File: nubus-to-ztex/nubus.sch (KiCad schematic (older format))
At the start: 46 parts, among them J4 C96ABC, U1 74LVT125, U12 74CB3T1G125DBVR, U13 SN74CB3T3125PWR, U14 SN74CB3T3245PWR, U2 74LVT125, U3 74LVT125, U4 SN74CB3T3125PWR, U5 74LVT245BPW,118, U6 74LVT245BPW,118, U7 74LVT245BPW,118, U8 74LVT245BPW,118

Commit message: cleanups, alternative MPN for 2x32 headers (TBC)
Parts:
- J4: MPN 85003-0567 -> 0850030567; MPN alias (none) -> 85003-0567
- U12: value 74CB3T1G125DBVR -> SN74CB3T1G125DBVR; MPN 74CB3T1G125DBVR -> SN74CB3T1G125DBVR
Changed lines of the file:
@@
 F 2 "For_SeeedStudio:DIN41612_C_3x32_Male_Horizontal_THT" H 22250 5800 50  0001 C CNN
 F 3 " ~" H 22250 5800 50  0001 C CNN
-F 4 "85003-0567" H 22250 5750 50  0001 C CNN "MPN"
+F 4 "85003-0567" H 22250 5750 50  0001 C CNN "MPN alias"
 F 5 "https://www.mouser.fr/ProductDetail/Molex/85003-0567?qs=U4pz39agNJB6P1oBpJ4bJA%3D%3D" H 22250 5750 50  0001 C CNN "URL"
 F 6 "DIN-096CPC-RR1-HM" H 22250 5750 50  0001 C CNN "MPN (3M)"
@@
 F 8 "09033967921" H 22250 5750 50  0001 C CNN "MPN (Harting)"
 F 9 "09033966921" H 22250 5750 50  0001 C CNN "MPN (Harting 2)"
+F 10 "0850030567" H 22250 5750 50  0001 C CNN "MPN"
 	1    22250 5750
 	1    0    0    -1
@@
 P 7450 13450
 F 0 "U12" H 7450 13767 50  0000 C CNN
-F 1 "74CB3T1G125DBVR" H 7450 13676 50  0000 C CNN
+F 1 "SN74CB3T1G125DBVR" H 7450 13676 50  0000 C CNN
 F 2 "Package_TO_SOT_SMD:SOT-23-5" H 7450 13450 50  0001 C CNN
 F 3 "http://www.ti.com/lit/sg/scyt129e/scyt129e.pdf" H 7450 13450 50  0001 C CNN
-F 4 "74CB3T1G125DBVR" H 7450 13450 50  0001 C CNN "MPN"
+F 4 "SN74CB3T1G125DBVR" H 7450 13450 50  0001 C CNN "MPN"
 F 5 "https://www.lcsc.com/product-detail/Analog-Switches-Multiplexers_Texas-Instruments-SN74CB3T1G125DBVR_C134001.html" H 7450 13450 50  0001 C CNN "URL"
 	1    7450 13450

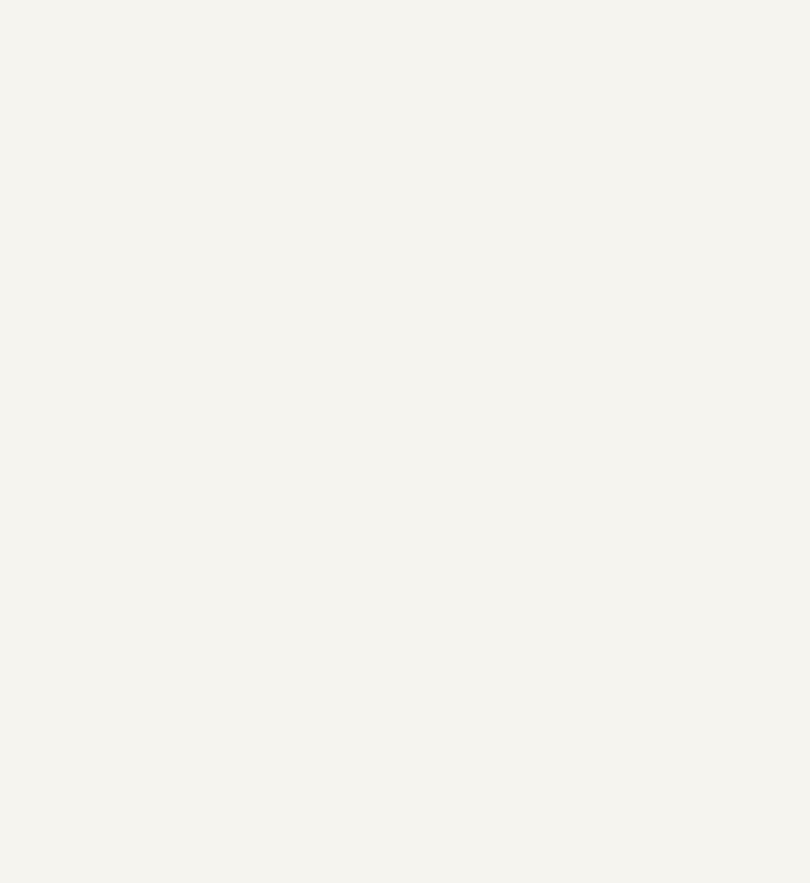
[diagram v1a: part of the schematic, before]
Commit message: reinstate some useful debug LEDs
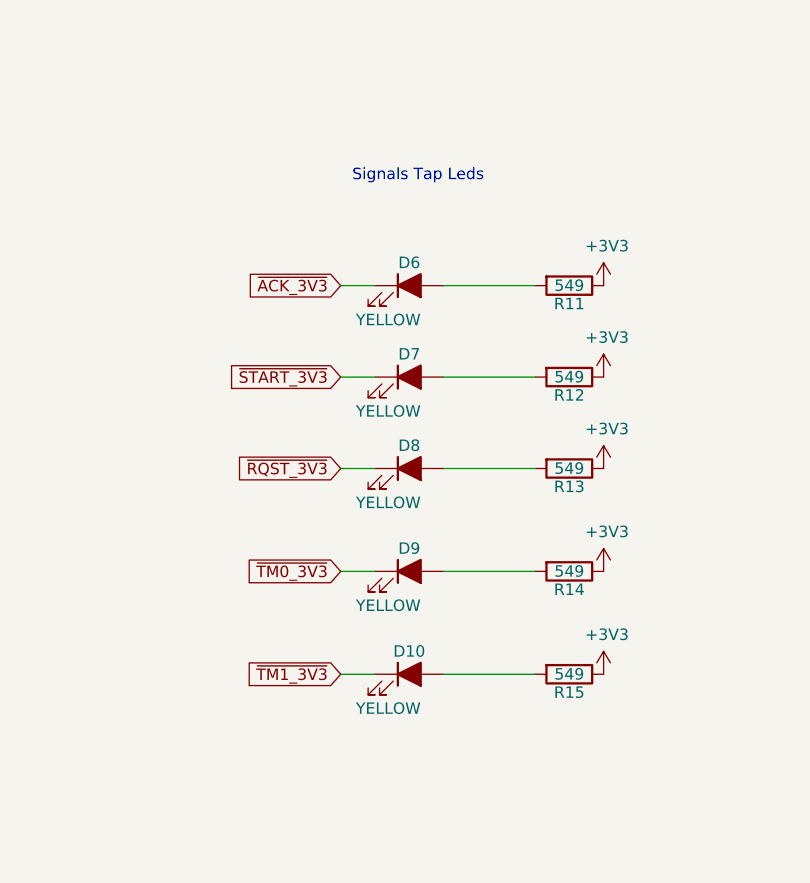
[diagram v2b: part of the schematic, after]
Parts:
- added D10, D6, D7, D8, D9: YELLOW, LED_SMD:LED_0805_2012Metric, symbol Device:LED_ALT
- added R11, R12, R13, R14, R15: 549, Resistor_SMD:R_0603_1608Metric, symbol Device:R
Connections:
- wire segments 54 -> 64
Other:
- note added: "Signals Tap Leds"

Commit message: cut down brightness of LEDs, more 2x32 pin headers reference
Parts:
- R11, R12, R13, R14, R15, R16, R17, R18, R19: value 549 -> 590; MPN 0603WAF5490T5E -> 0603WAF5900T5E; URL https://lcsc.com/product-detail/Chip-Resistor-Surface-Mount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 -> https://www.lcsc.com/product-detail/Chip-Resistor-Surface-M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
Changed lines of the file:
@@
 $Descr A2 23386 16535
 encoding utf-8
-Sheet 3 9
+Sheet 3 10
 Title "nubus-to-ztex NuBus connection & level shifting"
 Date ""
@@
 AR Path="/618F532C/61D85DF0" Ref="R16"  Part="1"
 F 0 "R16" V 16830 7850 50  0000 C CNN
-F 1 "549" V 16750 7850 50  0000 C CNN
+F 1 "590" V 16750 7850 50  0000 C CNN
 F 2 "Resistor_SMD:R_0603_1608Metric" V 16680 7850 50  0001 C CNN
 F 3 "" H 16750 7850 50  0000 C CNN
-F 4 "0603WAF5490T5E" V 16750 7850 50  0001 C CNN "MPN"
-F 5 "https://lcsc.com/product-detail/Chip-Resistor-Surface-Mount_UNI-ROYAL-Uniroyal-Elec-0603WAF5490T5E_C23079.html" V 16750 7850 50  0001 C CNN "URL"
+F 4 "0603WAF5900T5E" V 16750 7850 50  0001 C CNN "MPN"
+F 5 "https://www.lcsc.com/product-detail/Chip-Resistor-Surface-Mount_UNI-ROYAL-Uniroyal-Elec-0603WAF5900T5E_C23084.html" V 16750 7850 50  0001 C CNN "URL"
 	1    16750 7850
 	0    1    1    0
@@
 AR Path="/618F532C/61D85E0D" Ref="R17"  Part="1"
 F 0 "R17" V 16830 8350 50  0000 C CNN
-F 1 "549" V 16750 8350 50  0000 C CNN
+F 1 "590" V 16750 8350 50  0000 C CNN
 F 2 "Resistor_SMD:R_0603_1608Metric" V 16680 8350 50  0001 C CNN
 F 3 "" H 16750 8350 50  0000 C CNN
-F 4 "0603WAF5490T5E" V 16750 8350 50  0001 C CNN "MPN"
-F 5 "https://lcsc.com/product-detail/Chip-Resistor-Surface-Mount_UNI-ROYAL-Uniroyal-Elec-0603WAF5490T5E_C23079.html" V 16750 8350 50  0001 C CNN "URL"
+F 4 "0603WAF5900T5E" V 16750 8350 50  0001 C CNN "MPN"
+F 5 "https://www.lcsc.com/product-detail/Chip-Resistor-Surface-Mount_UNI-ROYAL-Uniroyal-Elec-0603WAF5900T5E_C23084.html" V 16750 8350 50  0001 C CNN "URL"
 	1    16750 8350
 	0    1    1    0
@@
 AR Path="/618F532C/61D85E2A" Ref="R18"  Part="1"
 F 0 "R18" V 16830 8850 50  0000 C CNN
-F 1 "549" V 16750 8850 50  0000 C CNN
+F 1 "590" V 16750 8850 50  0000 C CNN
 F 2 "Resistor_SMD:R_0603_1608Metric" V 16680 8850 50  0001 C CNN
 F 3 "" H 16750 8850 50  0000 C CNN
-F 4 "0603WAF5490T5E" V 16750 8850 50  0001 C CNN "MPN"
-F 5 "https://lcsc.com/product-detail/Chip-Resistor-Surface-Mount_UNI-ROYAL-Uniroyal-Elec-0603WAF5490T5E_C23079.html" V 16750 8850 50  0001 C CNN "URL"
+F 4 "0603WAF5900T5E" V 16750 8850 50  0001 C CNN "MPN"
+F 5 "https://www.lcsc.com/product-detail/Chip-Resistor-Surface-Mount_UNI-ROYAL-Uniroyal-Elec-0603WAF5900T5E_C23084.html" V 16750 8850 50  0001 C CNN "URL"
 	1    16750 8850
 	0    1    1    0
@@
 AR Path="/618F532C/61D85E47" Ref="R19"  Part="1"
 F 0 "R19" V 16830 9350 50  0000 C CNN
-F 1 "549" V 16750 9350 50  0000 C CNN
+F 1 "590" V 16750 9350 50  0000 C CNN
 F 2 "Resistor_SMD:R_0603_1608Metric" V 16680 9350 50  0001 C CNN
 F 3 "" H 16750 9350 50  0000 C CNN
-F 4 "0603WAF5490T5E" V 16750 9350 50  0001 C CNN "MPN"
-F 5 "https://lcsc.com/product-detail/Chip-Resistor-Surface-Mount_UNI-ROYAL-Uniroyal-Elec-0603WAF5490T5E_C23079.html" V 16750 9350 50  0001 C CNN "URL"
+F 4 "0603WAF5900T5E" V 16750 9350 50  0001 C CNN "MPN"
+F 5 "https://www.lcsc.com/product-detail/Chip-Resistor-Surface-Mount_UNI-ROYAL-Uniroyal-Elec-0603WAF5900T5E_C23084.html" V 16750 9350 50  0001 C CNN "URL"
 	1    16750 9350
 	0    1    1    0
@@
 AR Path="/6332A9A8/6332F9A9" Ref="R?"  Part="1"
 F 0 "R11" V 13780 7750 50  0000 C CNN
-F 1 "549" V 13700 7750 50  0000 C CNN
+F 1 "590" V 13700 7750 50  0000 C CNN
 F 2 "Resistor_SMD:R_0603_1608Metric" V 13630 7750 50  0001 C CNN
 F 3 "" H 13700 7750 50  0000 C CNN
-F 4 "0603WAF5490T5E" V 13700 7750 50  0001 C CNN "MPN"
-F 5 "https://lcsc.com/product-detail/Chip-Resistor-Surface-Mount_UNI-ROYAL-Uniroyal-Elec-0603WAF5490T5E_C23079.html" V 13700 7750 50  0001 C CNN "URL"
+F 4 "0603WAF5900T5E" V 13700 7750 50  0001 C CNN "MPN"
+F 5 "https://www.lcsc.com/product-detail/Chip-Resistor-Surface-Mount_UNI-ROYAL-Uniroyal-Elec-0603WAF5900T5E_C23084.html" V 13700 7750 50  0001 C CNN "URL"
 	1    13700 7750
 	0    1    1    0
@@
 AR Path="/6332A9A8/6334203F" Ref="R?"  Part="1"
 F 0 "R14" V 13780 9000 50  0000 C CNN
-F 1 "549" V 13700 9000 50  0000 C CNN
+F 1 "590" V 13700 9000 50  0000 C CNN
 F 2 "Resistor_SMD:R_0603_1608Metric" V 13630 9000 50  0001 C CNN
 F 3 "" H 13700 9000 50  0000 C CNN
-F 4 "0603WAF5490T5E" V 13700 9000 50  0001 C CNN "MPN"
-F 5 "https://lcsc.com/product-detail/Chip-Resistor-Surface-Mount_UNI-ROYAL-Uniroyal-Elec-0603WAF5490T5E_C23079.html" V 13700 9000 50  0001 C CNN "URL"
+F 4 "0603WAF5900T5E" V 13700 9000 50  0001 C CNN "MPN"
+F 5 "https://www.lcsc.com/product-detail/Chip-Resistor-Surface-Mount_UNI-ROYAL-Uniroyal-Elec-0603WAF5900T5E_C23084.html" V 13700 9000 50  0001 C CNN "URL"
 	1    13700 9000
 	0    1    1    0
@@
 AR Path="/6332A9A8/6334334C" Ref="R?"  Part="1"
 F 0 "R15" V 13780 9450 50  0000 C CNN
-F 1 "549" V 13700 9450 50  0000 C CNN
+F 1 "590" V 13700 9450 50  0000 C CNN
 F 2 "Resistor_SMD:R_0603_1608Metric" V 13630 9450 50  0001 C CNN
 F 3 "" H 13700 9450 50  0000 C CNN
-F 4 "0603WAF5490T5E" V 13700 9450 50  0001 C CNN "MPN"
-F 5 "https://lcsc.com/product-detail/Chip-Resistor-Surface-Mount_UNI-ROYAL-Uniroyal-Elec-0603WAF5490T5E_C23079.html" V 13700 9450 50  0001 C CNN "URL"
+F 4 "0603WAF5900T5E" V 13700 9450 50  0001 C CNN "MPN"
+F 5 "https://www.lcsc.com/product-detail/Chip-Resistor-Surface-Mount_UNI-ROYAL-Uniroyal-Elec-0603WAF5900T5E_C23084.html" V 13700 9450 50  0001 C CNN "URL"
 	1    13700 9450
 	0    1    1    0
@@
 AR Path="/6332A9A8/6334A052" Ref="R?"  Part="1"
 F 0 "R12" V 13780 8150 50  0000 C CNN
-F 1 "549" V 13700 8150 50  0000 C CNN
+F 1 "590" V 13700 8150 50  0000 C CNN
 F 2 "Resistor_SMD:R_0603_1608Metric" V 13630 8150 50  0001 C CNN
 F 3 "" H 13700 8150 50  0000 C CNN
-F 4 "0603WAF5490T5E" V 13700 8150 50  0001 C CNN "MPN"
-F 5 "https://lcsc.com/product-detail/Chip-Resistor-Surface-Mount_UNI-ROYAL-Uniroyal-Elec-0603WAF5490T5E_C23079.html" V 13700 8150 50  0001 C CNN "URL"
+F 4 "0603WAF5900T5E" V 13700 8150 50  0001 C CNN "MPN"
+F 5 "https://www.lcsc.com/product-detail/Chip-Resistor-Surface-Mount_UNI-ROYAL-Uniroyal-Elec-0603WAF5900T5E_C23084.html" V 13700 8150 50  0001 C CNN "URL"
 	1    13700 8150
 	0    1    1    0
@@
 AR Path="/6332A9A8/63352DBD" Ref="R?"  Part="1"
 F 0 "R13" V 13780 8550 50  0000 C CNN
-F 1 "549" V 13700 8550 50  0000 C CNN
+F 1 "590" V 13700 8550 50  0000 C CNN
 F 2 "Resistor_SMD:R_0603_1608Metric" V 13630 8550 50  0001 C CNN
 F 3 "" H 13700 8550 50  0000 C CNN
-F 4 "0603WAF5490T5E" V 13700 8550 50  0001 C CNN "MPN"
-F 5 "https://lcsc.com/product-detail/Chip-Resistor-Surface-Mount_UNI-ROYAL-Uniroyal-Elec-0603WAF5490T5E_C23079.html" V 13700 8550 50  0001 C CNN "URL"
+F 4 "0603WAF5900T5E" V 13700 8550 50  0001 C CNN "MPN"
+F 5 "https://www.lcsc.com/product-detail/Chip-Resistor-Surface-Mount_UNI-ROYAL-Uniroyal-Elec-0603WAF5900T5E_C23084.html" V 13700 8550 50  0001 C CNN "URL"
 	1    13700 8550
 	0    1    1    0
@@
 Text GLabel 12700 8550 0    50   Input ~ 0
 ~RQST_3V3
+$Comp
+L power:GND #PWR0110
+U 1 1 633B34AD
+P 7450 13600
+F 0 "#PWR0110" H 7450 13350 50  0001 C CNN
+F 1 "GND" H 7455 13427 50  0000 C CNN
+F 2 "" H 7450 13600 50  0001 C CNN
+F 3 "" H 7450 13600 50  0001 C CNN
+	1    7450 13600
+	1    0    0    -1
+$EndComp
+$Comp
+L power:+3V3 #PWR0111
+U 1 1 633B3A1A
+P 7450 13300
+F 0 "#PWR0111" H 7450 13150 50  0001 C CNN
+F 1 "+3V3" H 7465 13473 50  0000 C CNN
+F 2 "" H 7450 13300 50  0001 C CNN
+F 3 "" H 7450 13300 50  0001 C CNN
+	1    7450 13300
+	1    0    0    -1
+$EndComp
 $EndSCHEMATC

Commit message: merge pmod & leds into an extended pmod on the outside. Also some BoM updates.
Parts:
- C11, C14, C17, C18, C19, C30, C4, C5, C6, C7, C8: URL (none) -> https://lcsc.com/product-detail/Multilayer-Ceramic-Capacito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
- U5, U6, U7, U8: MPN 74LVT245BPW,118 -> SN74LVT245BPWR; MPN - ALT (none) -> 74LVT245BPW,118; URL https://www.digikey.fr/fr/products/detail/nexperia-usa-inc/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 -> https://lcsc.com/product-detail/Receivers-Transceivers_Texa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; URL - ALT (none) -> https://www.digikey.fr/fr/products/detail/nexperia-usa-inc/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; URL - ALT - mouser (none) -> https://eu.mouser.com/ProductDetail/?qs=me8TqzrmIYVnC5%252B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; URL-mouser https://eu.mouser.com/ProductDetail/?qs=me8TqzrmIYVnC5%252B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 -> (none)
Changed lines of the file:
@@
 $Descr A2 23386 16535
 encoding utf-8
-Sheet 3 10
+Sheet 3 9
 Title "nubus-to-ztex NuBus connection & level shifting"
 Date ""
@@
 F 9 "?" H 17550 2500 50  0001 C CNN "Koncar"
 F 10 "TB" H 17550 2500 50  0001 C CNN "Side"
+F 11 "https://lcsc.com/product-detail/Multilayer-Ceramic-Capacitors-MLCC-SMD-SMT_YAGEO-CC0603KRX7R8BB104_C92490.html" H 3000 6050 50  0001 C CNN "URL"
 	1    17550 2500
 	1    0    0    -1
@@
 F 2 "For_SeeedStudio:TSSOP-20_4.4x6.5mm_P0.65mm_ForSeeedStudio" H 17350 3450 50  0001 C CNN
 F 3 "http://www.ti.com/lit/gpn/sn74LS245" H 17350 3450 50  0001 C CNN
-F 4 "https://eu.mouser.com/ProductDetail/?qs=me8TqzrmIYVnC5%252BK4SaiTg%3D%3D" H 17350 3450 50  0001 C CNN "URL-mouser"
-F 5 "74LVT245BPW,118" H 17350 3450 50  0001 C CNN "MPN"
-F 6 "https://www.digikey.fr/fr/products/detail/nexperia-usa-inc/74LVT245BPW-118/1231957" H 17350 3450 50  0001 C CNN "URL"
+F 4 "https://eu.mouser.com/ProductDetail/?qs=me8TqzrmIYVnC5%252BK4SaiTg%3D%3D" H 17350 3450 50  0001 C CNN "URL - ALT - mouser"
+F 5 "74LVT245BPW,118" H 17350 3450 50  0001 C CNN "MPN - ALT"
+F 6 "https://www.digikey.fr/fr/products/detail/nexperia-usa-inc/74LVT245BPW-118/1231957" H 17350 3450 50  0001 C CNN "URL - ALT"
+F 7 "SN74LVT245BPWR" H 17350 3450 50  0001 C CNN "MPN"
+F 8 "https://lcsc.com/product-detail/Receivers-Transceivers_Texas-Instruments-SN74LVT245BPWR_C74214.html" H 17350 3450 50  0001 C CNN "URL"
 	1    17350 3450
 	-1   0    0    -1
@@
 F 9 "?" H 15550 2500 50  0001 C CNN "Koncar"
 F 10 "TB" H 15550 2500 50  0001 C CNN "Side"
+F 11 "https://lcsc.com/product-detail/Multilayer-Ceramic-Capacitors-MLCC-SMD-SMT_YAGEO-CC0603KRX7R8BB104_C92490.html" H 3000 6050 50  0001 C CNN "URL"
 	1    15550 2500
 	1    0    0    -1
@@
 F 2 "For_SeeedStudio:TSSOP-20_4.4x6.5mm_P0.65mm_ForSeeedStudio" H 15350 3450 50  0001 C CNN
 F 3 "http://www.ti.com/lit/gpn/sn74LS245" H 15350 3450 50  0001 C CNN
-F 4 "74LVT245BPW,118" H 15350 3450 50  0001 C CNN "MPN"
-F 5 "https://eu.mouser.com/ProductDetail/?qs=me8TqzrmIYVnC5%252BK4SaiTg%3D%3D" H 15350 3450 50  0001 C CNN "URL-mouser"
-F 6 "https://www.digikey.fr/fr/products/detail/nexperia-usa-inc/74LVT245BPW-118/1231957" H 15350 3450 50  0001 C CNN "URL"
+F 4 "74LVT245BPW,118" H 15350 3450 50  0001 C CNN "MPN - ALT"
+F 5 "https://eu.mouser.com/ProductDetail/?qs=me8TqzrmIYVnC5%252BK4SaiTg%3D%3D" H 15350 3450 50  0001 C CNN "URL - ALT - mouser"
+F 6 "https://www.digikey.fr/fr/products/detail/nexperia-usa-inc/74LVT245BPW-118/1231957" H 15350 3450 50  0001 C CNN "URL - ALT"
+F 7 "SN74LVT245BPWR" H 15350 3450 50  0001 C CNN "MPN"
+F 8 "https://lcsc.com/product-detail/Receivers-Transceivers_Texas-Instruments-SN74LVT245BPWR_C74214.html" H 15350 3450 50  0001 C CNN "URL"
 	1    15350 3450
 	-1   0    0    -1
@@
 F 9 "?" H 13500 2500 50  0001 C CNN "Koncar"
 F 10 "TB" H 13500 2500 50  0001 C CNN "Side"
+F 11 "https://lcsc.com/product-detail/Multilayer-Ceramic-Capacitors-MLCC-SMD-SMT_YAGEO-CC0603KRX7R8BB104_C92490.html" H 3000 6050 50  0001 C CNN "URL"
 	1    13500 2500
 	1    0    0    -1
@@
 F 2 "For_SeeedStudio:TSSOP-20_4.4x6.5mm_P0.65mm_ForSeeedStudio" H 13300 3450 50  0001 C CNN
 F 3 "http://www.ti.com/lit/gpn/sn74LS245" H 13300 3450 50  0001 C CNN
-F 4 "74LVT245BPW,118" H 13300 3450 50  0001 C CNN "MPN"
-F 5 "https://eu.mouser.com/ProductDetail/?qs=me8TqzrmIYVnC5%252BK4SaiTg%3D%3D" H 13300 3450 50  0001 C CNN "URL-mouser"
-F 6 "https://www.digikey.fr/fr/products/detail/nexperia-usa-inc/74LVT245BPW-118/1231957" H 13300 3450 50  0001 C CNN "URL"
+F 4 "74LVT245BPW,118" H 13300 3450 50  0001 C CNN "MPN - ALT"
+F 5 "https://eu.mouser.com/ProductDetail/?qs=me8TqzrmIYVnC5%252BK4SaiTg%3D%3D" H 13300 3450 50  0001 C CNN "URL - ALT - mouser"
+F 6 "https://www.digikey.fr/fr/products/detail/nexperia-usa-inc/74LVT245BPW-118/1231957" H 13300 3450 50  0001 C CNN "URL - ALT"
+F 7 "SN74LVT245BPWR" H 13300 3450 50  0001 C CNN "MPN"
+F 8 "https://lcsc.com/product-detail/Receivers-Transceivers_Texas-Instruments-SN74LVT245BPWR_C74214.html" H 13300 3450 50  0001 C CNN "URL"
 	1    13300 3450
 	-1   0    0    -1
@@
 F 9 "?" H 11450 2500 50  0001 C CNN "Koncar"
 F 10 "TB" H 11450 2500 50  0001 C CNN "Side"
+F 11 "https://lcsc.com/product-detail/Multilayer-Ceramic-Capacitors-MLCC-SMD-SMT_YAGEO-CC0603KRX7R8BB104_C92490.html" H 3000 6050 50  0001 C CNN "URL"
 	1    11450 2500
 	1    0    0    -1
@@
 F 2 "For_SeeedStudio:TSSOP-20_4.4x6.5mm_P0.65mm_ForSeeedStudio" H 11250 3450 50  0001 C CNN
 F 3 "http://www.ti.com/lit/gpn/sn74LS245" H 11250 3450 50  0001 C CNN
-F 4 "74LVT245BPW,118" H 11250 3450 50  0001 C CNN "MPN"
-F 5 "https://eu.mouser.com/ProductDetail/?qs=me8TqzrmIYVnC5%252BK4SaiTg%3D%3D" H 11250 3450 50  0001 C CNN "URL-mouser"
+F 4 "74LVT245BPW,118" H 11250 3450 50  0001 C CNN "MPN - ALT"
+F 5 "https://eu.mouser.com/ProductDetail/?qs=me8TqzrmIYVnC5%252BK4SaiTg%3D%3D" H 11250 3450 50  0001 C CNN "URL - ALT - mouser"
 F 6 "https://www.renesas.com/us/en/package/pcg20" H 11250 3450 50  0001 C CNN "Drawings"
 F 7 "https://www.renesas.com/document/psc/pcpcg-package-outline-150-body-width-qsop-025-pitch?language=en" H 11250 3450 50  0001 C CNN "Datasheet - Packaging"
 F 8 "https://assets.nexperia.com/documents/package-information/SOT360-1.pdf" H 11250 3450 50  0001 C CNN "Package Drawings"
-F 9 "https://www.digikey.fr/fr/products/detail/nexperia-usa-inc/74LVT245BPW-118/1231957" H 11250 3450 50  0001 C CNN "URL"
+F 9 "https://www.digikey.fr/fr/products/detail/nexperia-usa-inc/74LVT245BPW-118/1231957" H 11250 3450 50  0001 C CNN "URL - ALT"
+F 10 "SN74LVT245BPWR" H 11250 3450 50  0001 C CNN "MPN"
+F 11 "https://lcsc.com/product-detail/Receivers-Transceivers_Texas-Instruments-SN74LVT245BPWR_C74214.html" H 11250 3450 50  0001 C CNN "URL"
 	1    11250 3450
 	-1   0    0    -1
@@
 F 9 "?" H 5100 6200 50  0001 C CNN "Koncar"
 F 10 "TB" H 5100 6200 50  0001 C CNN "Side"
+F 11 "https://lcsc.com/product-detail/Multilayer-Ceramic-Capacitors-MLCC-SMD-SMT_YAGEO-CC0603KRX7R8BB104_C92490.html" H 3000 6050 50  0001 C CNN "URL"
 	1    5100 6200
 	1    0    0    -1
@@
 F 9 "?" H 4650 2850 50  0001 C CNN "Koncar"
 F 10 "TB" H 4650 2850 50  0001 C CNN "Side"
+F 11 "https://lcsc.com/product-detail/Multilayer-Ceramic-Capacitors-MLCC-SMD-SMT_YAGEO-CC0603KRX7R8BB104_C92490.html" H 3000 6050 50  0001 C CNN "URL"
 	1    4650 2850
 	1    0    0    -1
@@
 F 9 "?" H 4700 10300 50  0001 C CNN "Koncar"
 F 10 "TB" H 4700 10300 50  0001 C CNN "Side"
+F 11 "https://lcsc.com/product-detail/Multilayer-Ceramic-Capacitors-MLCC-SMD-SMT_YAGEO-CC0603KRX7R8BB104_C92490.html" H 3000 6050 50  0001 C CNN "URL"
 	1    4700 10300
 	1    0    0    -1
@@
 F 9 "?" H 5150 13300 50  0001 C CNN "Koncar"
 F 10 "TB" H 5150 13300 50  0001 C CNN "Side"
+F 11 "https://lcsc.com/product-detail/Multilayer-Ceramic-Capacitors-MLCC-SMD-SMT_YAGEO-CC0603KRX7R8BB104_C92490.html" H 5150 13300 50  0001 C CNN "URL"
 	1    5150 13300
 	-1   0    0    -1
@@
 F 9 "?" H 10200 14650 50  0001 C CNN "Koncar"
 F 10 "TB" H 10200 14650 50  0001 C CNN "Side"
+F 11 "https://lcsc.com/product-detail/Multilayer-Ceramic-Capacitors-MLCC-SMD-SMT_YAGEO-CC0603KRX7R8BB104_C92490.html" H 3000 6050 50  0001 C CNN "URL"
 	1    10200 14650
 	1    0    0    -1
@@
 F 9 "?" H 13050 14650 50  0001 C CNN "Koncar"
 F 10 "TB" H 13050 14650 50  0001 C CNN "Side"
+F 11 "https://lcsc.com/product-detail/Multilayer-Ceramic-Capacitors-MLCC-SMD-SMT_YAGEO-CC0603KRX7R8BB104_C92490.html" H 3000 6050 50  0001 C CNN "URL"
 	1    13050 14650
 	1    0    0    -1
@@
 F 9 "?" H 7950 13850 50  0001 C CNN "Koncar"
 F 10 "TB" H 7950 13850 50  0001 C CNN "Side"
+F 11 "https://lcsc.com/product-detail/Multilayer-Ceramic-Capacitors-MLCC-SMD-SMT_YAGEO-CC0603KRX7R8BB104_C92490.html" H 3000 6050 50  0001 C CNN "URL"
 	1    7950 13850
 	-1   0    0    -1

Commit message: simplify BoM
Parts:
- removed C11, C7: 100nF, Capacitor_SMD:C_0603_1608Metric, symbol Device:C
- removed U12: SN74CB3T1G125DBVR, Package_TO_SOT_SMD:SOT-23-5, symbol 74xGxx:74CB3T1G125
- removed U13, U4: SN74CB3T3125PWR, Package_SO:TSSOP-14_4.4x5mm_P0.65mm, symbol ul_SN74CB3T3125PW:SN74CB3T3125PW
- added C12: 100nF, Capacitor_SMD:C_0603_1608Metric, symbol Device:C
- added U13, U15: SN74CB3T3245PWR, For_SeeedStudio:TSSOP-20_4.4x6.5mm_P0.65mm_ForSeeedStudio, symbol SN74CB3T3245PWR:SN74CB3T3245PWR
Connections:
- wire segments 64 -> 68
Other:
- note added: "How should unused input be connected ?"
- note added: "SN74CB3T3245PW are cheaper and more available than the SN74CB3T3125PW ..."
